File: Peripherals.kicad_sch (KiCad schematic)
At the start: 33 parts, among them J2 Conn_01x02, J5 Conn_01x03, J6 Conn_01x03, M1 Vibrator DC Motor, U10 BMI270, U12 DRV2603RUNR, U2 OPT3004DNPR, U5 W25Q32JVSS, U9 MAX30102EFD_T

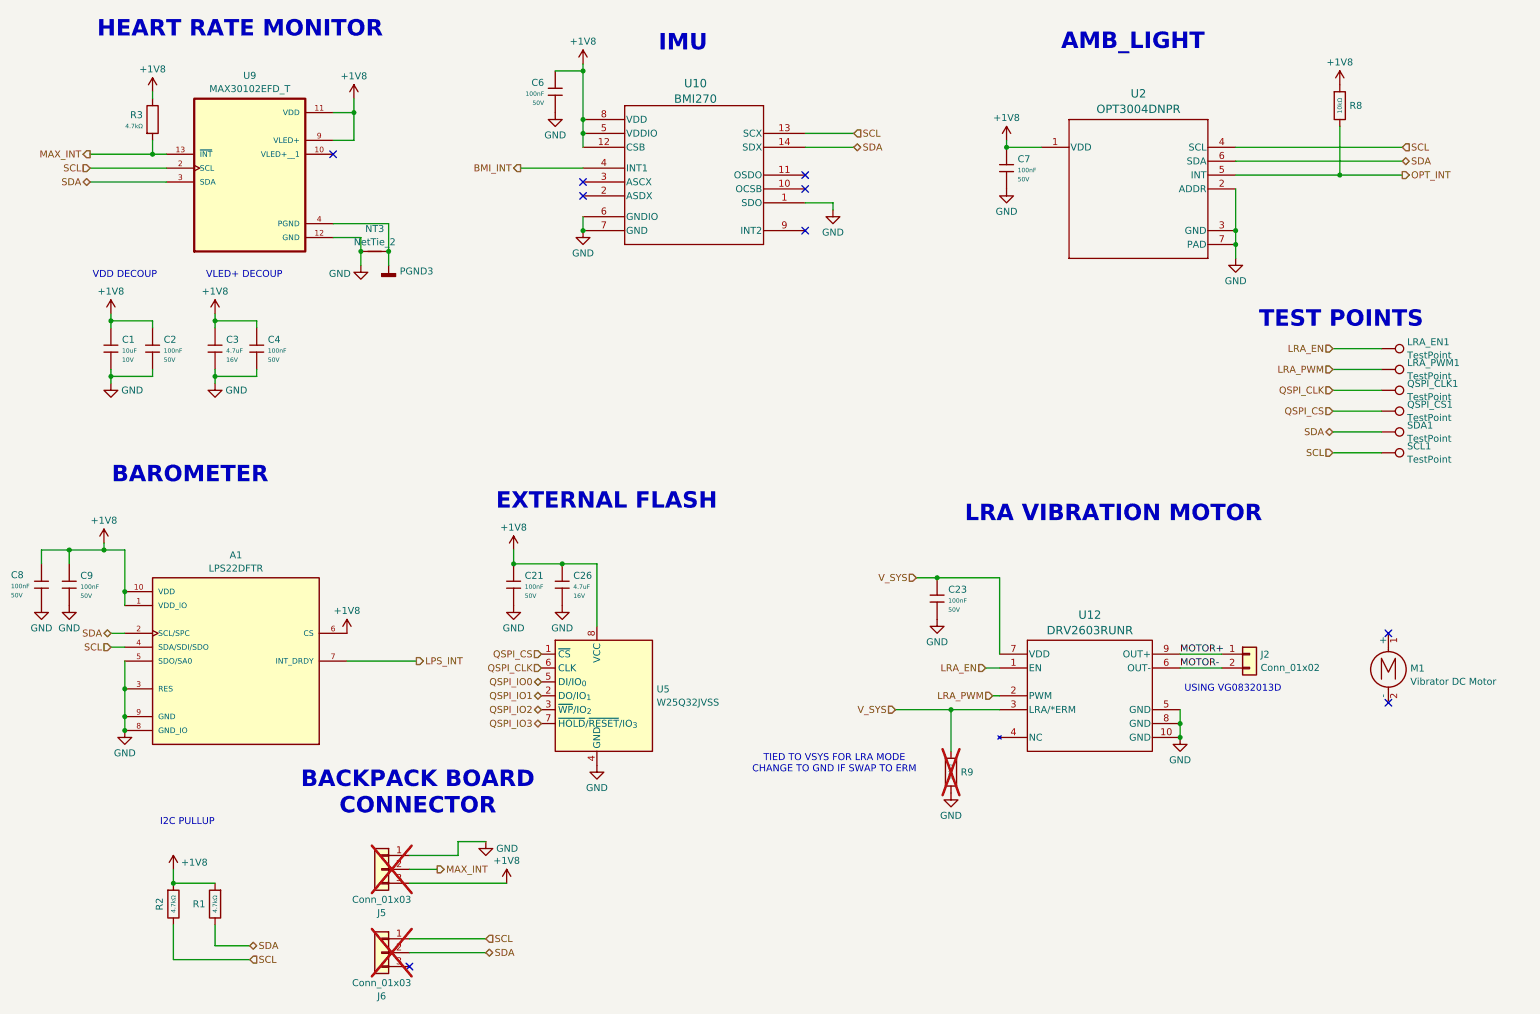
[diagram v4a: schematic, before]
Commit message: Removed amb light, extended board for usbc and buttons
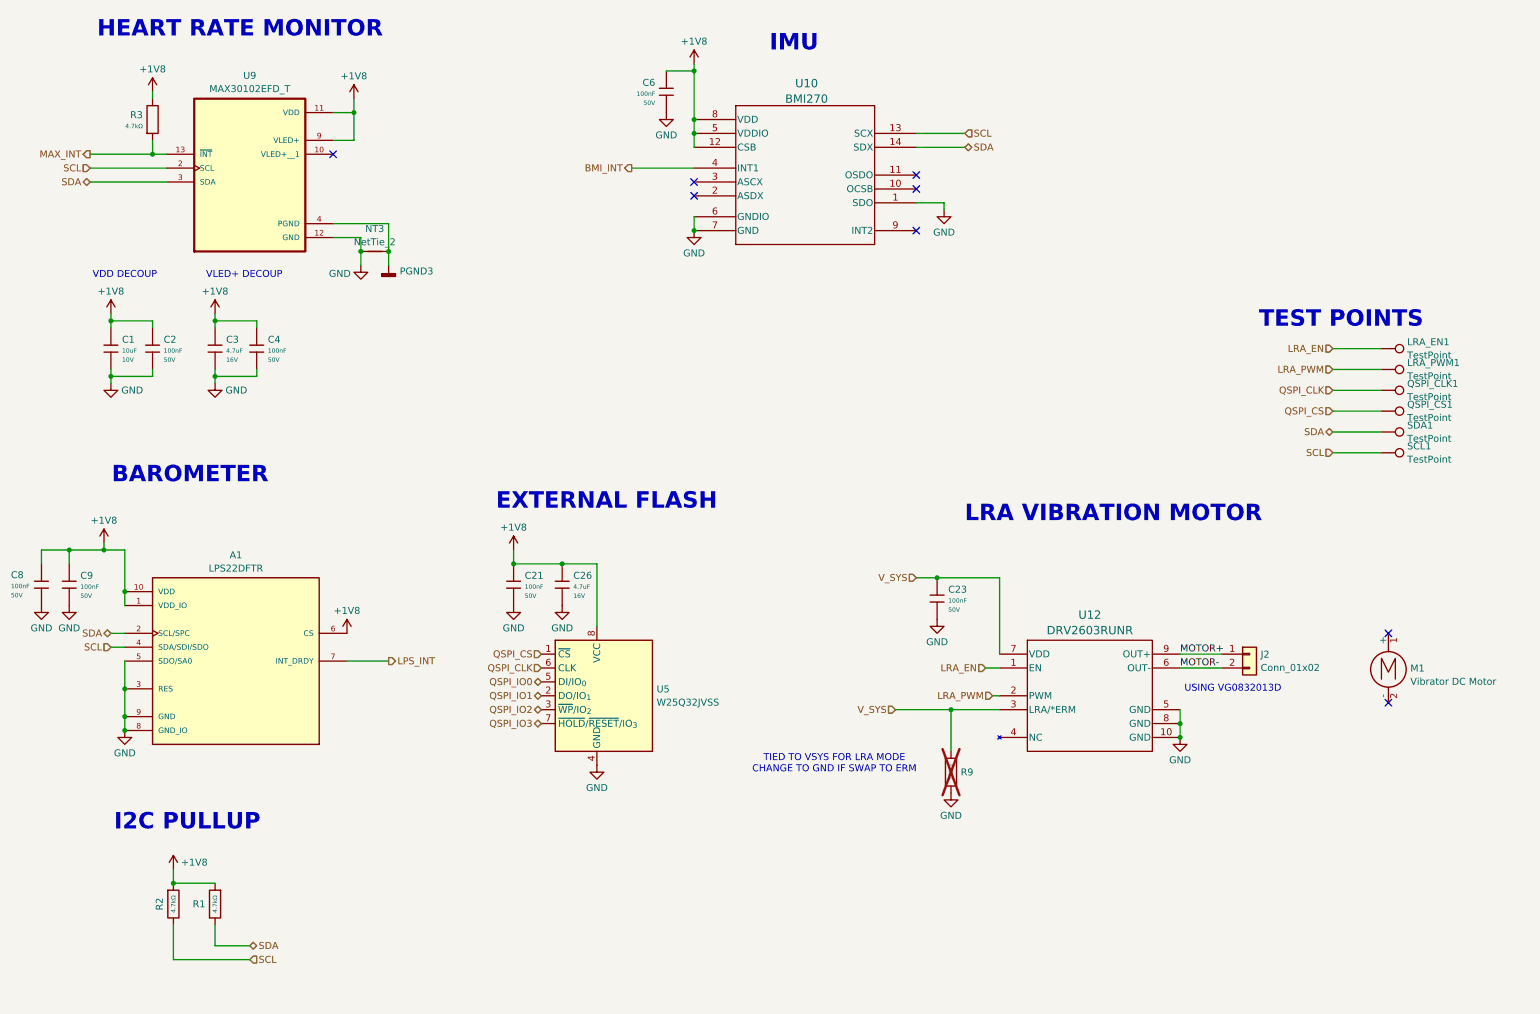
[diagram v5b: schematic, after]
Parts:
- removed C7: 100nF, PCM_JLCPCB:C_0603, symbol PCM_JLCPCB-Capacitors:0603,100nF
- removed J5, J6: Conn_01x03, Connector_PinHeader_1.27mm:PinHeader_1x03_P1.27mm_Vertical_SMD_Pin1Left, symbol Connector_Generic:Conn_01x03
- removed R8: 10kΩ, PCM_JLCPCB:R_0603, symbol PCM_JLCPCB-Resistors:0603,10kΩ
- removed U2: OPT3004DNPR, Smart_Watch:DNP0006A, symbol Smart_Watch:OPT3004DNPR
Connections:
- no-connect marks 9 -> 8
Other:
- note removed: "AMB_LIGHT"
- note removed: "BACKPACK BOARD CONNECTOR"
- moved on the sheet: C6, U10
